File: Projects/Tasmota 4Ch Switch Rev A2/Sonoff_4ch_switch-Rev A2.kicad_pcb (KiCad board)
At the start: 2 copper layers, 99.8 x 99.1 mm, 60 parts, among them J1 Barrel_Jack_Switch, J2 Live, J3 Neutrals, J4 Earths, J5 Conn_01x03_Male, K1 G5LE-1, K2 G5LE-1, K3 G5LE-1, K4 G5LE-1, Q1 2N7002, Q2 2N7002, Q3 2N7002, Q4 2N7002, Q5 2N7002, Q6 2N7002, Q7 2N7002, Q8 2N7002, U1 AP1117-50, U2 Wemos_D1_Mini_wide

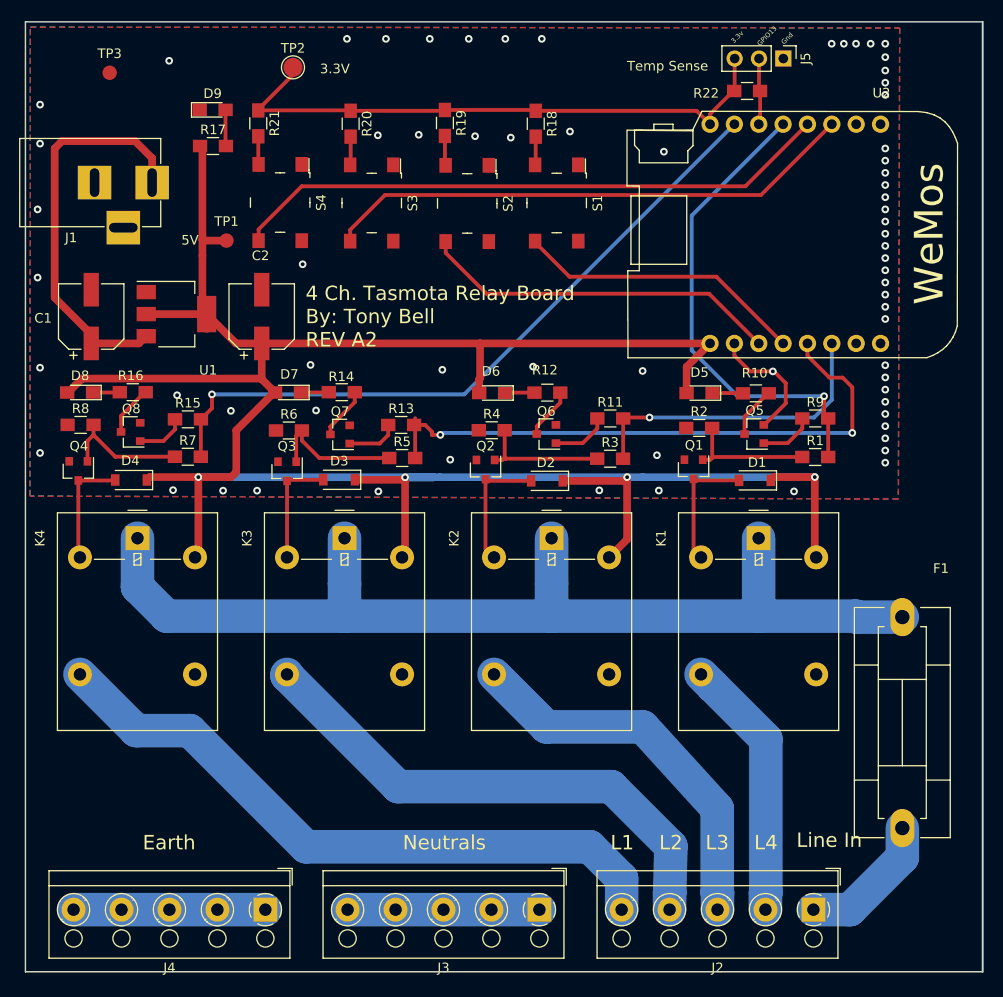
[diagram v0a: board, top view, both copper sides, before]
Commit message: Created new 2Ch Tasmota Switch
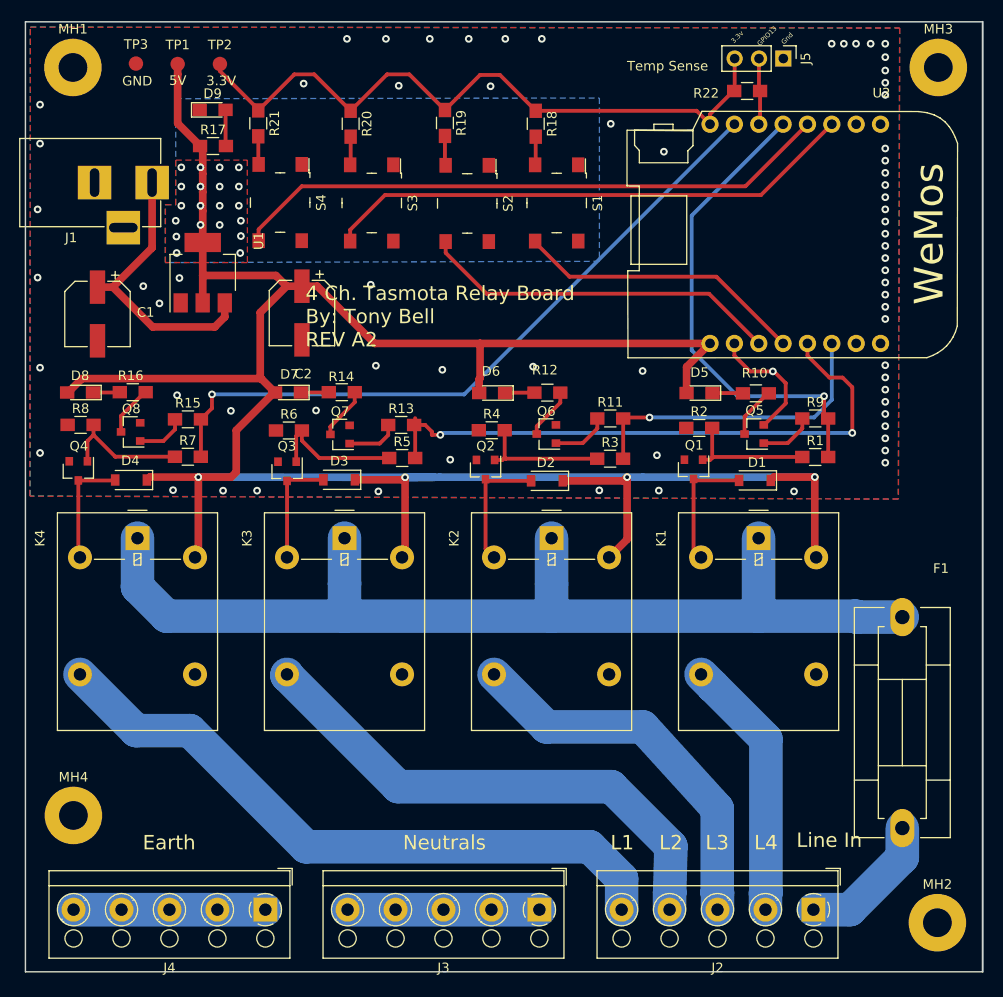
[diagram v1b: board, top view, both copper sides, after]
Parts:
- added MH1: MountingHole, Mounting_Holes:MountingHole_3mm_Pad, F.Cu at (86.0, 37.3)
- added MH2: MountingHole, Mounting_Holes:MountingHole_3mm_Pad, F.Cu at (176.1, 126.5)
- added MH3: MountingHole, Mounting_Holes:MountingHole_3mm_Pad, F.Cu at (176.2, 37.3)
- added MH4: MountingHole, Mounting_Holes:MountingHole_3mm_Pad, F.Cu at (86.0, 115.3)
- TP2: footprint TestPoint:TestPoint_Pad_D2.0mm -> Measurement_Points:Measurement_Point_Round-SMD-Pad_Small
- moved TP1 19.1 mm to (96.9, 36.9)
- moved TP2 7.63 mm to (101.3, 36.9)
- moved U1 5.11 mm to (99.5, 58.7), turned to 90 degrees
- moved C2 4.21 mm to (109.9, 62.9), turned to 270 degrees
- moved TP3 2.91 mm to (92.6, 36.9)
- moved C1 0.71 mm to (88.5, 63.0), turned to 270 degrees
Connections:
- S1 pad 1: GND -> Net-(S1-Pad1)
- S2 pad 1: GND -> Net-(S2-Pad1)
- S3 pad 1: GND -> Net-(S3-Pad1)
- S4 pad 1: GND -> Net-(S4-Pad1)
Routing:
- net /DC_IN: track 41.7 -> 29.5 mm
- net +3V3: track 61.7 -> 71.5 mm
- net +5V: track 262.9 -> 269.6 mm, vias 4 -> 24
- net GND: vias 70 -> 71
- added copper zone on B.Cu, net +5V
- added copper zone on F.Cu, net +5V
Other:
- board text added: "GND"
